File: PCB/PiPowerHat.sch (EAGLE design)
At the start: 29 parts, among them IC1 7805T, K1 PIN20X2, U1 EEPROM24, U2 INA219AIDCNRSOIC, U4 DS18B20

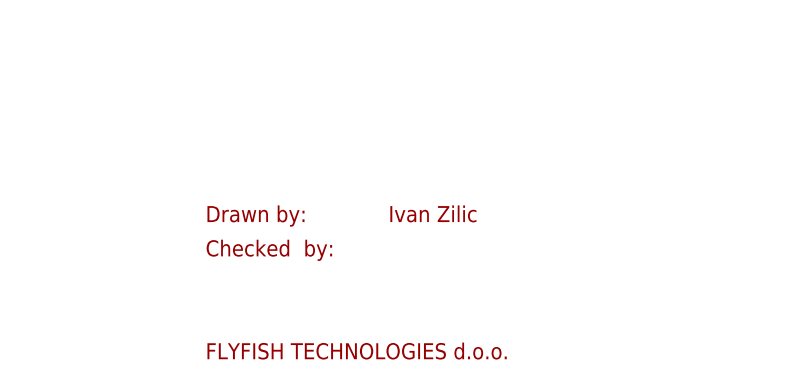
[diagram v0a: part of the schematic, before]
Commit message: Corrected dimension measurements to be on the measurements layer, not dimensions.
Added Version and name/date.

Printed schema and PCB to PDFs

Added readme.
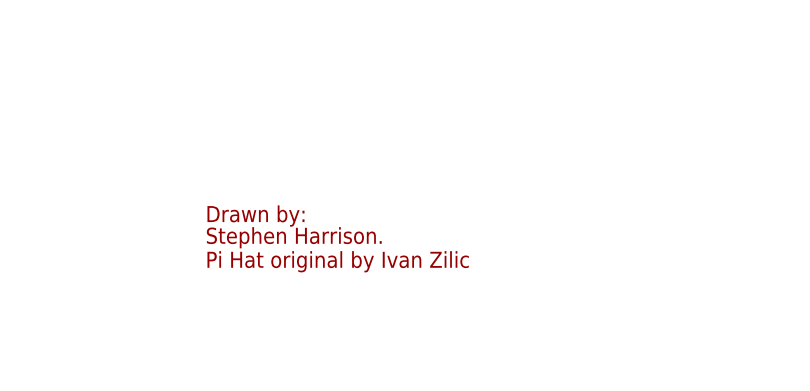
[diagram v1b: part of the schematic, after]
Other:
- note added: "Stephen Harrison. Pi Hat original by Ivan Zilic"
- note removed: "Checked by:"
- note removed: "FLYFISH TECHNOLOGIES d.o.o."
- note removed: "Ivan Zilic"
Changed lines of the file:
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@@
 <plain>
 <text x="289.56" y="20.32" size="1.778" layer="94" ratio="15">Drawn by:</text>
-<text x="289.56" y="16.51" size="1.778" layer="94" ratio="15">Checked  by:</text>
-<text x="289.56" y="5.08" size="1.778" layer="94">FLYFISH TECHNOLOGIES d.o.o.</text>
-<text x="309.88" y="20.32" size="1.778" layer="94">Ivan Zilic</text>
+<text x="289.56" y="15.24" size="1.778" layer="94">Stephen Harrison.
+Pi Hat original by Ivan Zilic</text>
 <text x="374.65" y="5.08" size="2.54" layer="94" ratio="10">v0.1</text>
 <text x="170.18" y="223.52" size="1.27" layer="97">SOIC 8 temp sensor to monitor PCB/Ambient.</text>

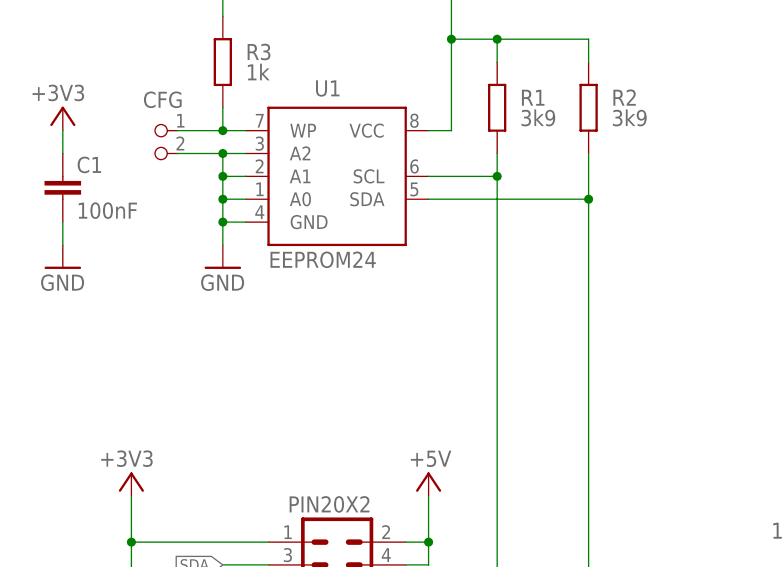
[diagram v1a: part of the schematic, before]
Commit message: Added notes for eeprom
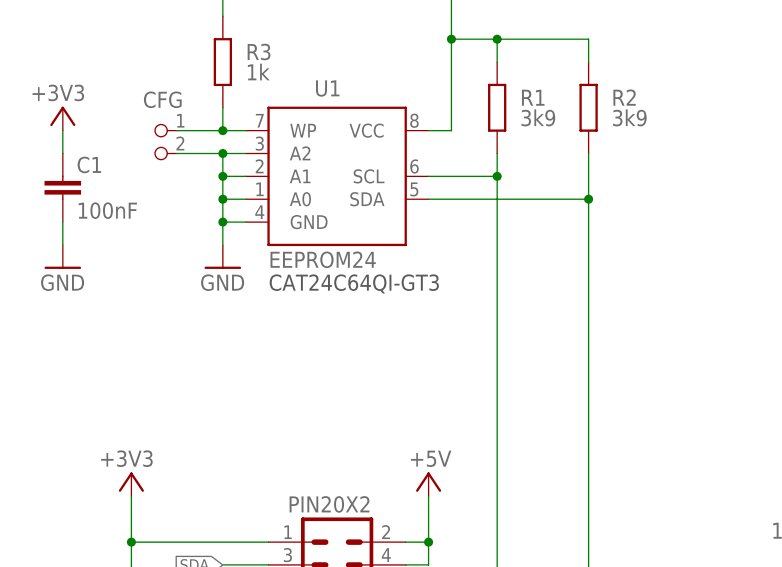
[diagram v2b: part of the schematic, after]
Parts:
- U1: FARNELL (none) -> 2463718
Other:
- note added: "CAT24C64QI-GT3"
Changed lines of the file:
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@@
 <part name="K1" library="FLYFISH" deviceset="PIN20X2" device=""/>
 <part name="FRAME1" library="frames" deviceset="A3L-LOC" device=""/>
-<part name="U1" library="FLYFISH" deviceset="EEPROM24" device=""/>
+<part name="U1" library="FLYFISH" deviceset="EEPROM24" device="">
+<attribute name="FARNELL" value="2463718"/>
+</part>
 <part name="GND10" library="supply1" deviceset="GND" device=""/>
 <part name="R1" library="resistor" deviceset="R-EU_" device="M0805" value="3k9">
@@
 <text x="170.18" y="223.52" size="1.27" layer="97">SOIC 8 temp sensor to monitor PCB/Ambient.</text>
 <text x="297.18" y="223.52" size="1.27" layer="97">External DB18B20 to monitor ambient</text>
+<text x="43.18" y="203.2" size="1.778" layer="97">CAT24C64QI-GT3</text>
 </plain>
 <instances>
@@
 <attribute name="NAME" x="48.26" y="224.79" size="1.778" layer="95"/>
 <attribute name="VALUE" x="43.18" y="205.74" size="1.778" layer="96"/>
+<attribute name="FARNELL" x="50.8" y="215.9" size="1.778" layer="96" display="off"/>
 </instance>
 <instance part="GND10" gate="1" x="60.96" y="121.92"/>

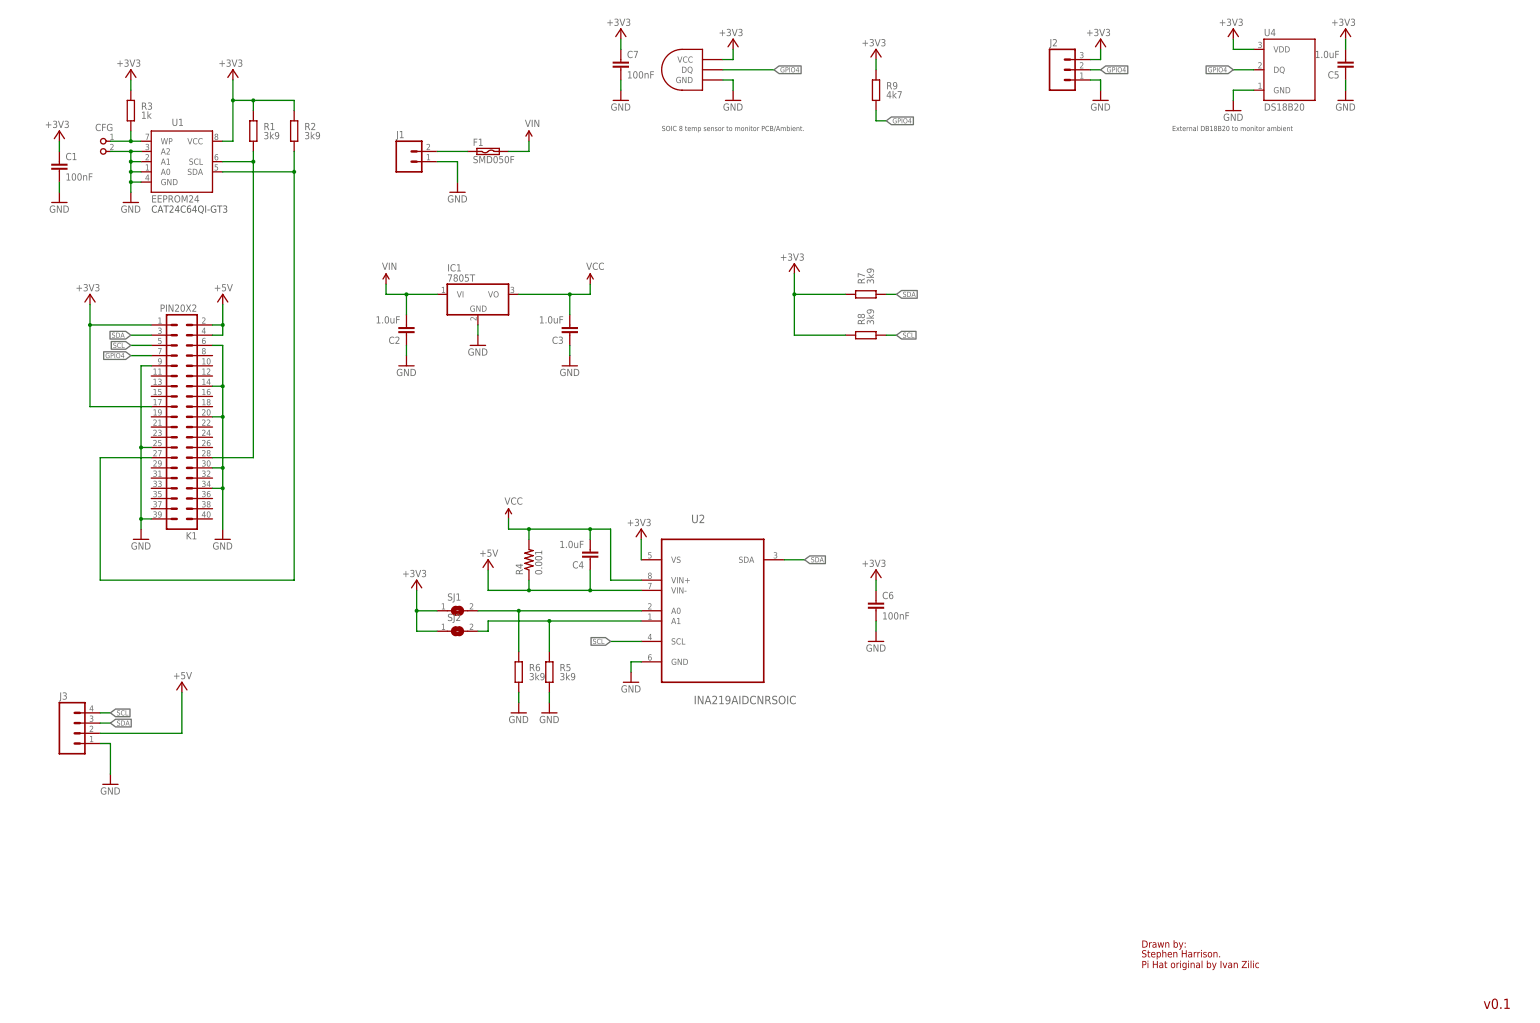
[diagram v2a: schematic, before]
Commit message: Tidied up schematic/board with feedback from 1st build.
Added BOM.
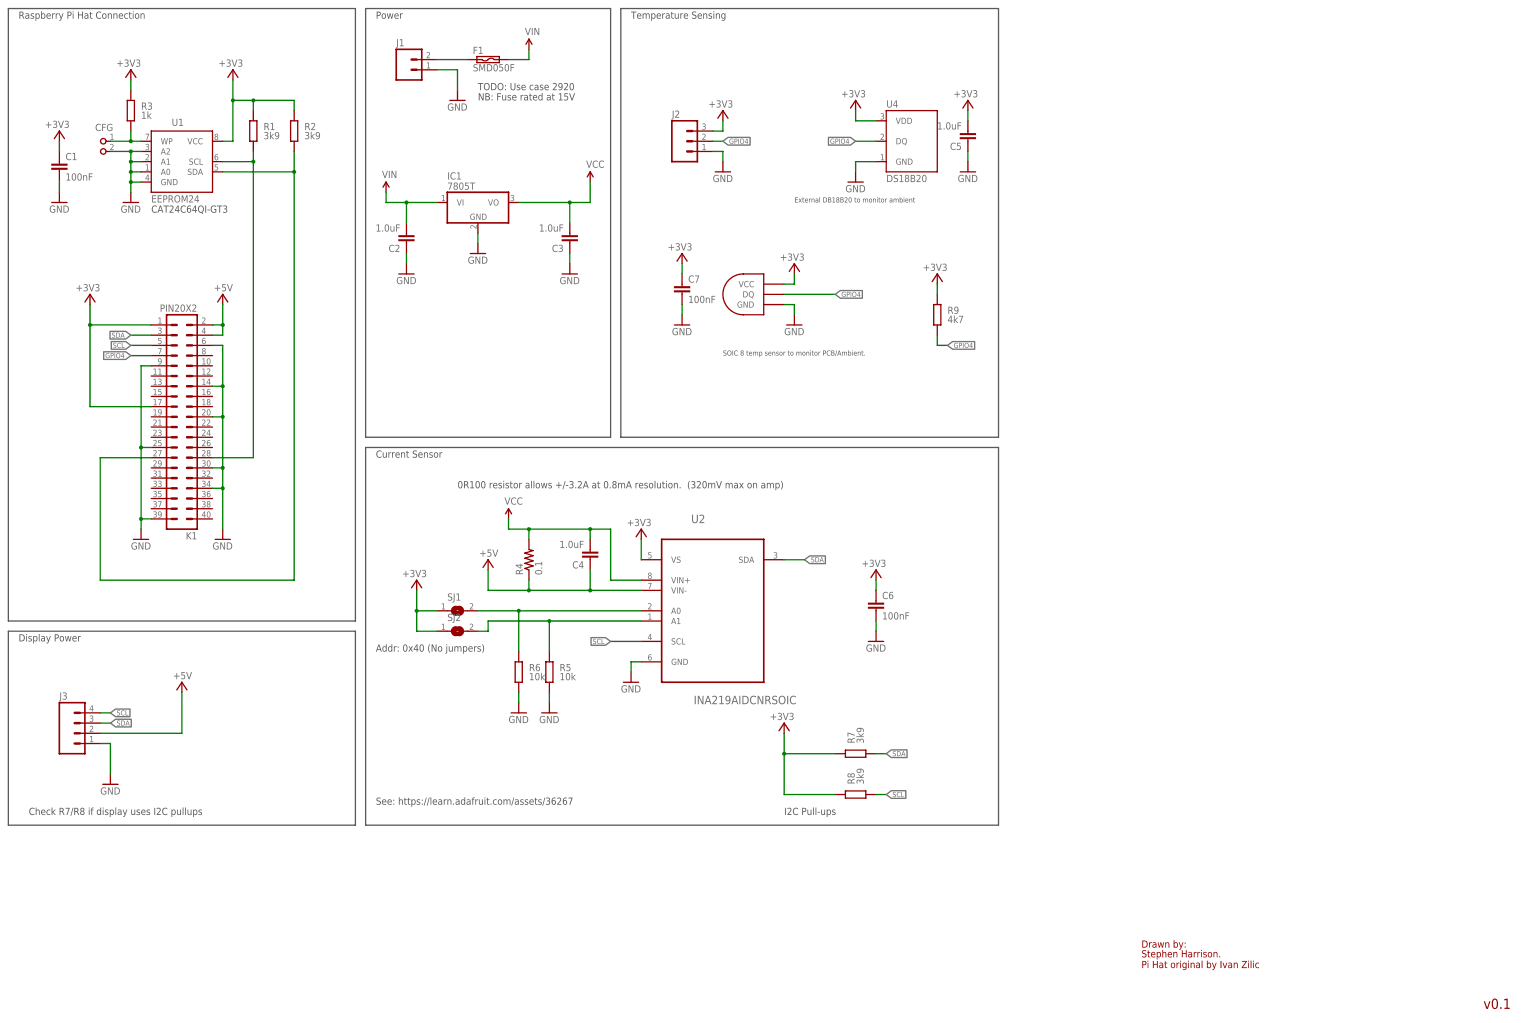
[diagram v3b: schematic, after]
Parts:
- removed U$1: DS1820SOIC, DS1820-SOIC:DS1820SOIC
- added U5: DS1820SOIC, DS1820-SOIC:DS1820SOIC
- R4: value 0.001 -> 0.1
- R5, R6: value 3k9 -> 10k
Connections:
- net +3V3: now also U5.VCC; no longer U$1.VCC
- net GND: now also U5.GND; no longer U$1.GND
- net GPIO4: now also U5.DQ; no longer U$1.DQ
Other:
- note added: "0R100 resistor allows +/-3.2A at 0.8mA resolution. (320mV max on amp)"
- note added: "Addr: 0x40 (No jumpers)"
- note added: "Check R7/R8 if display uses I2C pullups"
- note added: "Current Sensor"
- note added: "Display Power"
- note added: "I2C Pull-ups"
- note added: "NB: Fuse rated at 15V"
- note added: "Power"
- note added: "Raspberry Pi Hat Connection"
- note added: "See: https://learn.adafruit.com/assets/36267"
- note added: "TODO: Use case 2920"
- note added: "Temperature Sensing"
- moved on the sheet: C2, C3, C5, C7, F1, IC1, J1, J2, R7, R8, R9, U4

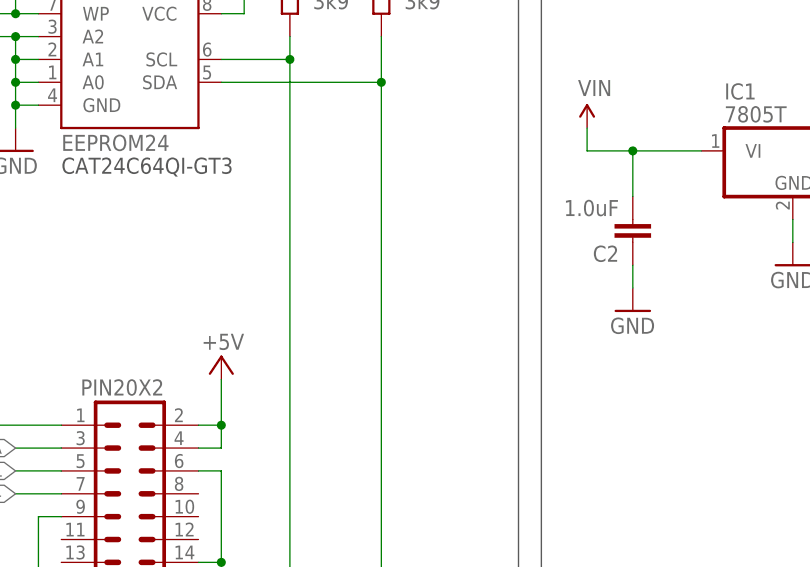
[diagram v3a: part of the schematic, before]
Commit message: Improved routing to not use bottom layer so much
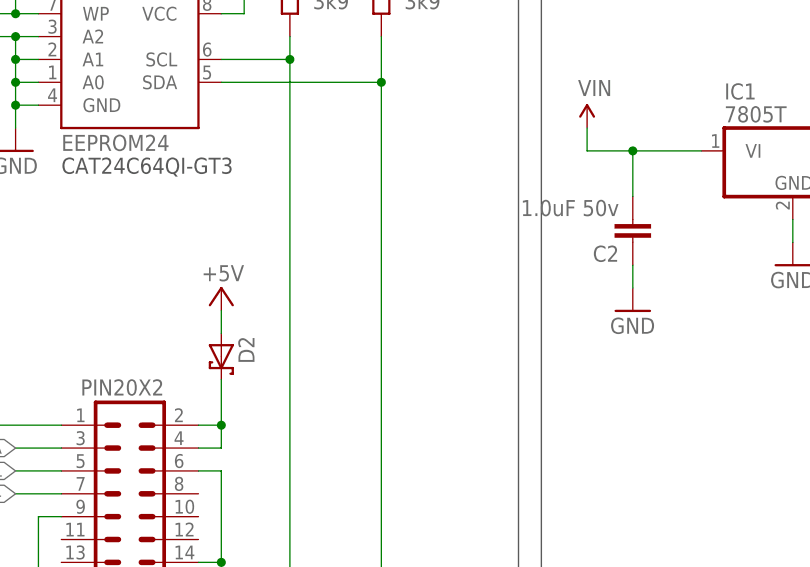
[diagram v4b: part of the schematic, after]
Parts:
- added D2: (no value), diode:SCHOTTKY-DIODESMC
- C2: value 1.0uF -> 1.0uF 50v
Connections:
- new net N$2: D2.C, K1.2, K1.4
- net +5V: now also D2.A; no longer K1.2, K1.4
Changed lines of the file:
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@@
 <part name="GND2" library="supply1" deviceset="GND" device=""/>
 <part name="GND3" library="supply1" deviceset="GND" device=""/>
-<part name="P+1" library="supply1" deviceset="+5V" device=""/>
 <part name="U2" library="INA219AIDCNR" deviceset="INA219AIDCNR" device="SOIC"/>
 <part name="IC1" library="linear" deviceset="78*" device="T" technology="05"/>
-<part name="C2" library="SparkFun-Capacitors" deviceset="1.0UF-25V-+80/-20(0805)" device="&quot;" value="1.0uF"/>
+<part name="C2" library="SparkFun-Capacitors" deviceset="1.0UF-25V-+80/-20(0805)" device="&quot;" value="1.0uF 50v"/>
 <part name="C3" library="SparkFun-Capacitors" deviceset="1.0UF-25V-+80/-20(0805)" device="&quot;" value="1.0uF"/>
 <part name="C4" library="SparkFun-Capacitors" deviceset="1.0UF-25V-+80/-20(0805)" device="&quot;" value="1.0uF"/>
@@
 </part>
 <part name="+3V14" library="supply1" deviceset="+3V3" device=""/>
+<part name="D2" library="diode" deviceset="SCHOTTKY-DIODE" device="SMC"/>
+<part name="P+1" library="supply1" deviceset="+5V" device=""/>
 </parts>
 <sheets>
@@
 <instance part="GND2" gate="1" x="20.32" y="205.74"/>
 <instance part="GND3" gate="1" x="40.64" y="121.92"/>
-<instance part="P+1" gate="1" x="60.96" y="182.88" smashed="yes">
-<attribute name="VALUE" x="63.5" y="185.42" size="1.778" layer="96" rot="R180"/>
-</instance>
 <instance part="U2" gate="A" x="182.88" y="106.68"/>
 <instance part="IC1" gate="A1" x="124.46" y="205.74"/>
@@
 <instance part="+3V14" gate="G$1" x="238.76" y="187.96" smashed="yes">
 <attribute name="VALUE" x="241.3" y="190.5" size="1.778" layer="96" rot="R180"/>
+</instance>
+<instance part="D2" gate="G$1" x="60.96" y="182.88" rot="R270"/>
+<instance part="P+1" gate="1" x="60.96" y="190.5" smashed="yes">
+<attribute name="VALUE" x="63.5" y="193.04" size="1.778" layer="96" rot="R180"/>
 </instance>
 </instances>
@@
 <net name="+5V" class="0">
 <segment>
-<pinref part="K1" gate="G$1" pin="2"/>
-<pinref part="P+1" gate="1" pin="+5V"/>
-<wire x1="58.42" y1="175.26" x2="60.96" y2="175.26" width="0.1524" layer="91"/>
-<wire x1="60.96" y1="175.26" x2="60.96" y2="180.34" width="0.1524" layer="91"/>
-<pinref part="K1" gate="G$1" pin="4"/>
-<wire x1="58.42" y1="172.72" x2="60.96" y2="172.72" width="0.1524" layer="91"/>
-<wire x1="60.96" y1="172.72" x2="60.96" y2="175.26" width="0.1524" layer="91"/>
-<junction x="60.96" y="175.26"/>
-</segment>
-<segment>
 <pinref part="U2" gate="A" pin="VIN-"/>
 <wire x1="165.1" y1="109.22" x2="152.4" y2="109.22" width="0.1524" layer="91"/>
@@
 <wire x1="50.8" y1="73.66" x2="50.8" y2="83.82" width="0.1524" layer="91"/>
 <pinref part="P+3" gate="1" pin="+5V"/>
+</segment>
+<segment>
+<pinref part="P+1" gate="1" pin="+5V"/>
+<pinref part="D2" gate="G$1" pin="A"/>
+<wire x1="60.96" y1="187.96" x2="60.96" y2="185.42" width="0.1524" layer="91"/>
 </segment>
 </net>
@@
 </segment>
 </net>
+<net name="N$2" class="0">
+<segment>
+<pinref part="K1" gate="G$1" pin="2"/>
+<wire x1="58.42" y1="175.26" x2="60.96" y2="175.26" width="0.1524" layer="91"/>
+<wire x1="60.96" y1="175.26" x2="60.96" y2="180.34" width="0.1524" layer="91"/>
+<pinref part="K1" gate="G$1" pin="4"/>
+<wire x1="58.42" y1="172.72" x2="60.96" y2="172.72" width="0.1524" layer="91"/>
+<wire x1="60.96" y1="172.72" x2="60.96" y2="175.26" width="0.1524" layer="91"/>
+<junction x="60.96" y="175.26"/>
+<pinref part="D2" gate="G$1" pin="C"/>
+</segment>
+</net>
